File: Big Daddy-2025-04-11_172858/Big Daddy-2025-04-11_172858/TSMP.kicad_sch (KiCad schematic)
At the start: 7 parts, among them J3 HV+, J4 HV-, J5 GND, J6 HV+, J7 HV-

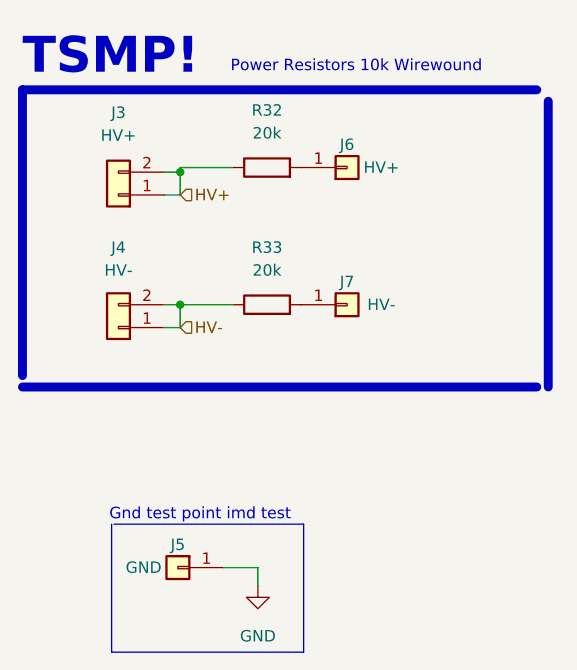
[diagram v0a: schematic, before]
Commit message: fixed HV connections to TSMP and HV-in
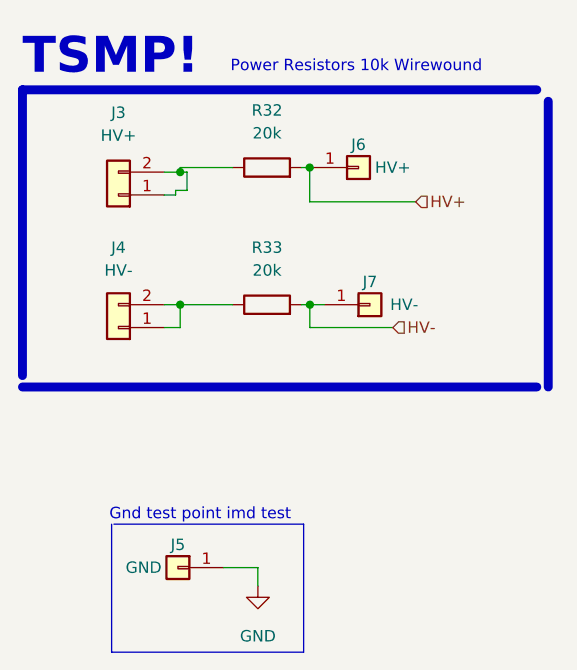
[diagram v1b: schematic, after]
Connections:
- net HV+: now also J6.1 (Pin_1), R32.2; no longer J3.1 (Pin_1), J3.2 (Pin_2), R32.1
- net HV-: now also J7.1 (Pin_1), R33.2; no longer J4.1 (Pin_1), J4.2 (Pin_2), R33.1
- new net: J3.1 (Pin_1), J3.2 (Pin_2), R32.1
- new net: J4.1 (Pin_1), J4.2 (Pin_2), R33.1
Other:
- moved on the sheet: J6, J7
